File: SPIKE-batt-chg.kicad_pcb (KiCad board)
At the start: 2 copper layers, 174.5 x 30 mm, 123 parts, among them IC1 CH224K, IC2 CN3702, IC3 CN3702, IC4 CN3702, J1 USB_C_Receptacle_USB2.0, J2 Barrel_Jack_Switch, J3 Conn_01x03_Pin, J4 Conn_01x03_Pin, J5 Conn_01x03_Pin, J6 Conn_01x01_Pin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

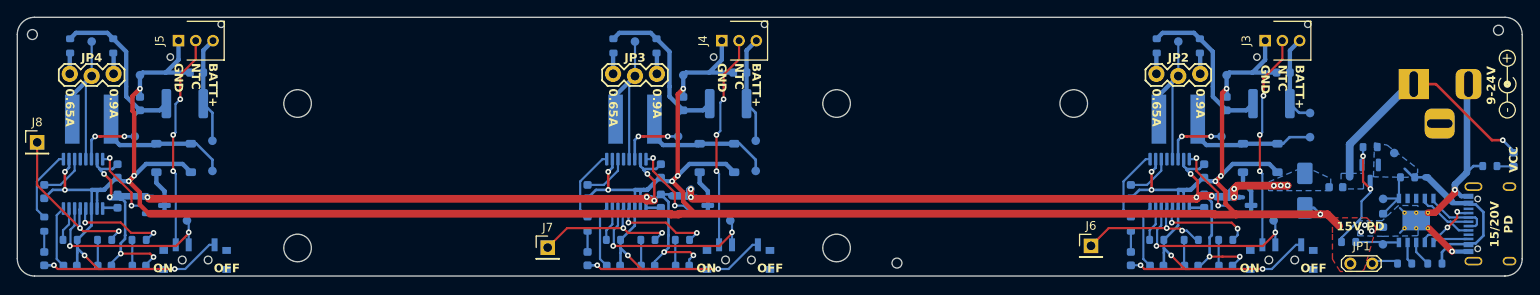
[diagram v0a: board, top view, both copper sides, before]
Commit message: Fix the routing for rotated MOSFET
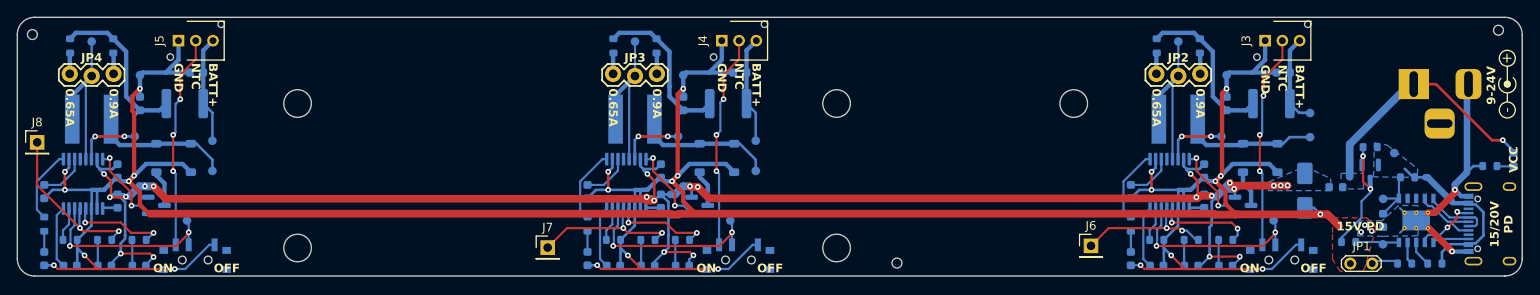
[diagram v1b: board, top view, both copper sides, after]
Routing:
- net Net-(D12-A): track 5.18 -> 4.24 mm
- net Net-(D8-A): track 5.18 -> 4.24 mm
- net Net-(D4-A): track 5.18 -> 4.24 mm
- net /CN3702 Charger1/VCC: track 214.5 -> 214.7 mm, vias 22 -> 24

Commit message: fixes, drc check
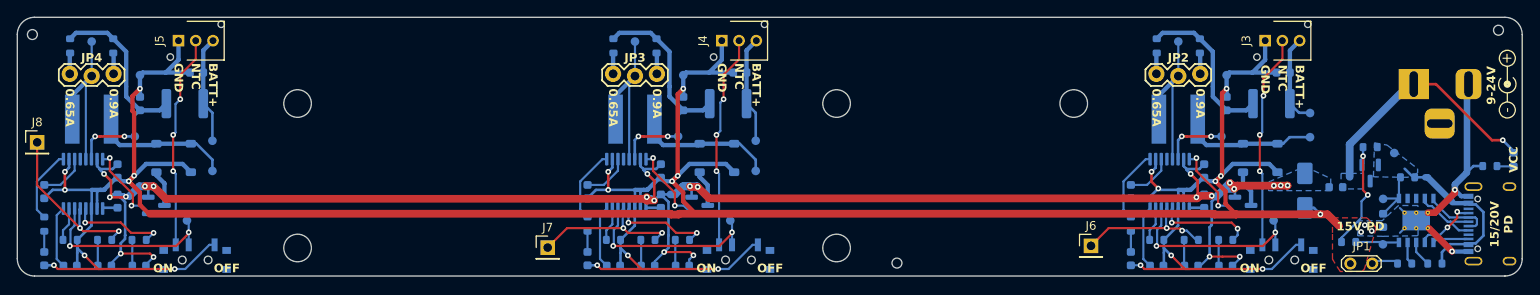
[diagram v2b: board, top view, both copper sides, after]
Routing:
- net /CN3702 Charger1/VCC: track 214.7 -> 218.8 mm

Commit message: fill zones, generated updated gerber and BOM
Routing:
- net VCC: track 29.1 -> 30.5 mm
